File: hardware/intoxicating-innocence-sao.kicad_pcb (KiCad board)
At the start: 2 copper layers, 36 x 32 mm, 5 parts, among them J1 SAO

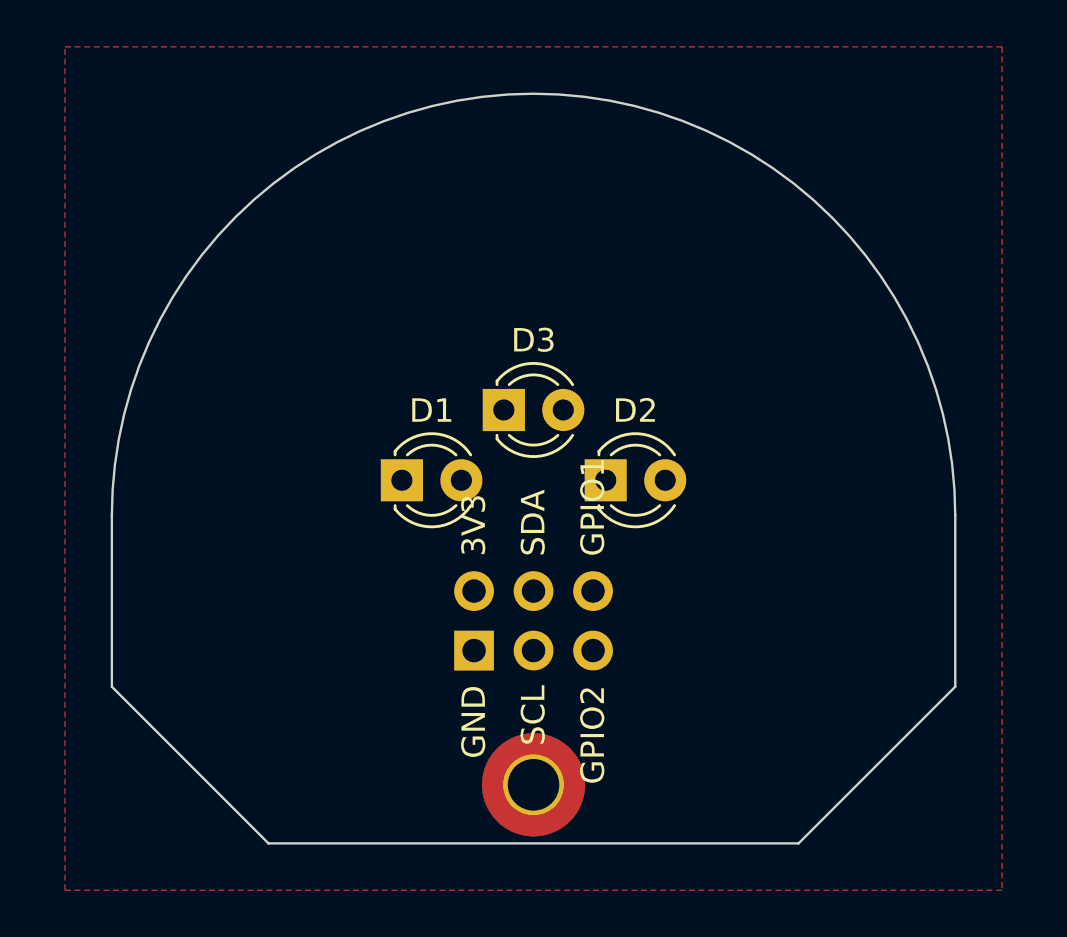
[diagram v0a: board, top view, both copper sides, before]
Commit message: Route shape-noninforming PCB components
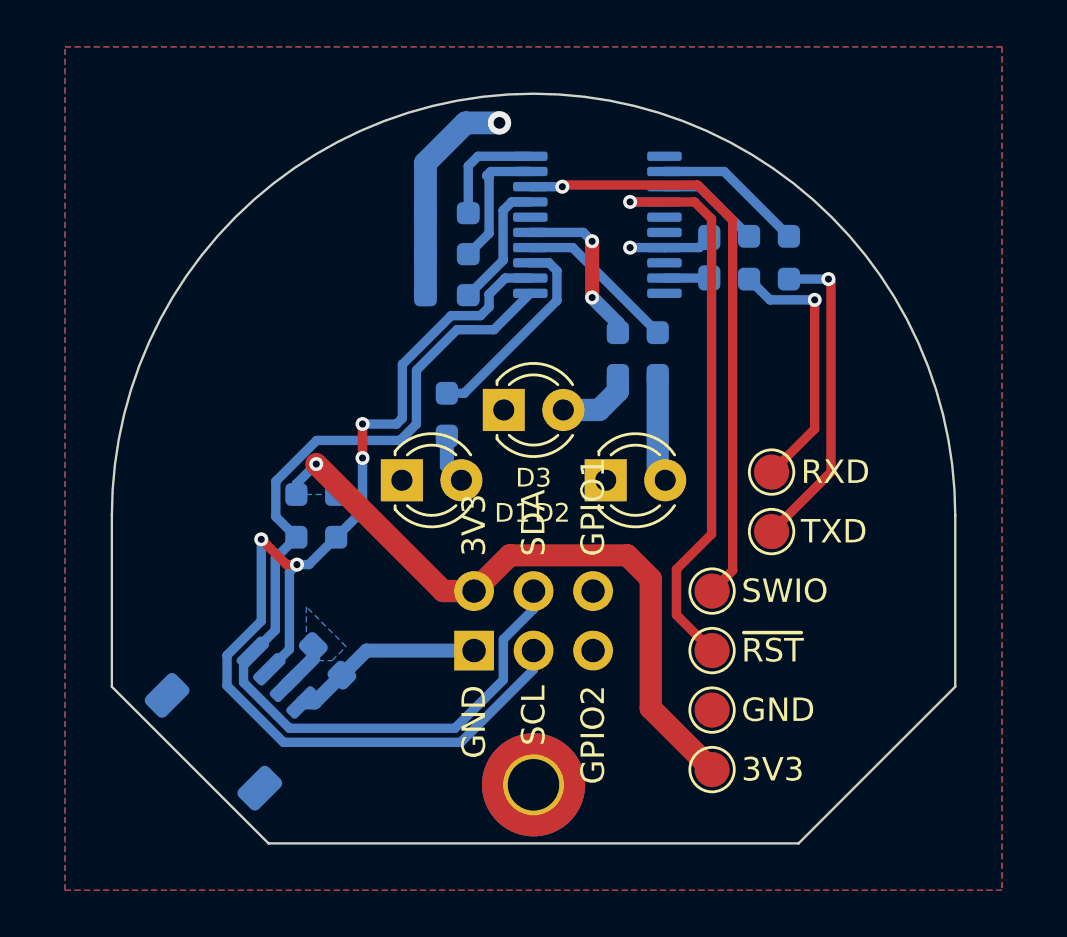
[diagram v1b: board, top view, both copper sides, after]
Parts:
- added C1: 10uF, Capacitor_SMD:C_0603_1608Metric_Pad1.08x0.95mm_HandSolder, B.Cu at (91.2, 106.2)
- added C2: 100nF, Capacitor_SMD:C_0603_1608Metric_Pad1.08x0.95mm_HandSolder, B.Cu at (107.5, 89.0)
- added J2: QWIIC, Connector_JST:JST_SH_SM04B-SRSS-TB_1x04-1MP_P1.00mm_Horizontal, B.Cu at (87.7, 108.3)
- added QWIIC_Front: QWIIC_Front, kantoniak-kicad:qwiic_logo, B.Cu at (84.9, 104.4)
- added R1: 10k, Resistor_SMD:R_0603_1608Metric_Pad0.98x0.95mm_HandSolder, B.Cu at (89.9, 100.0)
- added R10: 10k, Resistor_SMD:R_0603_1608Metric_Pad0.98x0.95mm_HandSolder, B.Cu at (96.3, 87.1)
- added R2: 10k, Resistor_SMD:R_0603_1608Metric_Pad0.98x0.95mm_HandSolder, B.Cu at (91.6, 100.0)
- added R3: 330, Resistor_SMD:R_0603_1608Metric_Pad0.98x0.95mm_HandSolder, B.Cu at (110.9, 89.0)
- added R4: 330, Resistor_SMD:R_0603_1608Metric_Pad0.98x0.95mm_HandSolder, B.Cu at (109.2, 89.0)
- added R5: 330, Resistor_SMD:R_0603_1608Metric_Pad0.98x0.95mm_HandSolder, B.Cu at (96.3, 95.7)
- added R6: 330, Resistor_SMD:R_0603_1608Metric_Pad0.98x0.95mm_HandSolder, B.Cu at (105.3, 93.1)
- added R7: 330, Resistor_SMD:R_0603_1608Metric_Pad0.98x0.95mm_HandSolder, B.Cu at (103.6, 93.1)
- added R8: 10k, Resistor_SMD:R_0603_1608Metric_Pad0.98x0.95mm_HandSolder, B.Cu at (96.3, 90.6)
- added R9: 10k, Resistor_SMD:R_0603_1608Metric_Pad0.98x0.95mm_HandSolder, B.Cu at (96.3, 88.8)
- added TP1: 3V3, TestPoint:TestPoint_Pad_D1.5mm, F.Cu at (107.6, 110.8)
- added TP2: GND, TestPoint:TestPoint_Pad_D1.5mm, F.Cu at (107.6, 108.3)
- added TP3: SWIO, TestPoint:TestPoint_Pad_D1.5mm, F.Cu at (107.6, 103.2)
- added TP4: ~{RST}, TestPoint:TestPoint_Pad_D1.5mm, F.Cu at (107.6, 105.8)
- added TP5: TXD, TestPoint:TestPoint_Pad_D1.5mm, F.Cu at (110.2, 100.7)
- added TP6: RXD, TestPoint:TestPoint_Pad_D1.5mm, F.Cu at (110.2, 98.2)
- added U1: CH32V003F4P6, Package_SO:TSSOP-20_4.4x6.5mm_P0.65mm, B.Cu at (102.7, 87.6)
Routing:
- net SCL: track 0.00 -> 48.8 mm, vias 0 -> 4
- net SDA: track 0.00 -> 42.5 mm
- net +3V3: track 0.00 -> 33.7 mm, vias 0 -> 1
- net SWIO: track 0.00 -> 25.5 mm, vias 0 -> 1
- net ~{RST}: track 0.00 -> 24.9 mm, vias 0 -> 1
- net GND: track 0.00 -> 21.3 mm, vias 0 -> 2
- net UART_TX: track 0.00 -> 13.6 mm, vias 0 -> 1
- net UART_RX: track 0.00 -> 11.3 mm, vias 0 -> 1
- net LED_LEFT: track 0.00 -> 8.89 mm
- net LED_TOP: track 0.00 -> 7.15 mm, vias 0 -> 2
- net LED_RIGHT: track 0.00 -> 6.94 mm
- net Net-(U1-PD5): track 0.00 -> 6.46 mm
- net CONFIG_B: track 0.00 -> 5.69 mm
- net CONFIG_A: track 0.00 -> 5.54 mm
- net CONFIG_C: track 0.00 -> 4.83 mm
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- added copper zone on B.Cu, net +3V3
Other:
- board text added: "A"
- board text added: "B"
- board text added: "C"
- board text added: "CONFIG"

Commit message: Fix SCL/SDA routing, add I2C test pads
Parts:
- added TP7: SCL, TestPoint:TestPoint_Pad_D1.5mm, F.Cu at (92.4, 103.2)
- added TP8: SDA, TestPoint:TestPoint_Pad_D1.5mm, F.Cu at (92.4, 105.8)
- moved R1 1.72 mm to (91.6, 100.0)
- moved R2 1.70 mm to (89.9, 100.0)
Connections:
- J2 pad 3: SCL -> SDA
- J2 pad 4: SDA -> SCL
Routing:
- net SCL: track 48.8 -> 43.2 mm, vias 4 -> 1
- net SDA: track 42.5 -> 41.7 mm, vias 0 -> 1

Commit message: Finish silkscreens
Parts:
- moved QWIIC_Front 2.47 mm to (85.8, 102.1), turned to -45 degrees
- moved C2 0.66 mm to (107.5, 88.3)
- moved R3 0.66 mm to (110.9, 88.3)
- moved R4 0.66 mm to (109.2, 88.3)
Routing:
- net UART_RX: track 11.3 -> 9.30 mm
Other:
- board text added: "Come Nerevar, friend or traitor, come. Come and look upon the Heart"
- board text added: "GITHUB.COM/KANTONIAK/ INTOXICATING-INNOCENCE-SAO LICENSE: ${LICENSE} KANTONIAK.COM • REV${PROJECT_REVISION}"
- board text added: "GND"
